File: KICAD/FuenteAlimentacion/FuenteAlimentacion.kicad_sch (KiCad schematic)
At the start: 5 parts, among them J1 USB_B_Mini, U1 LM1117DT-3.3, U2 TPS61087DSCR

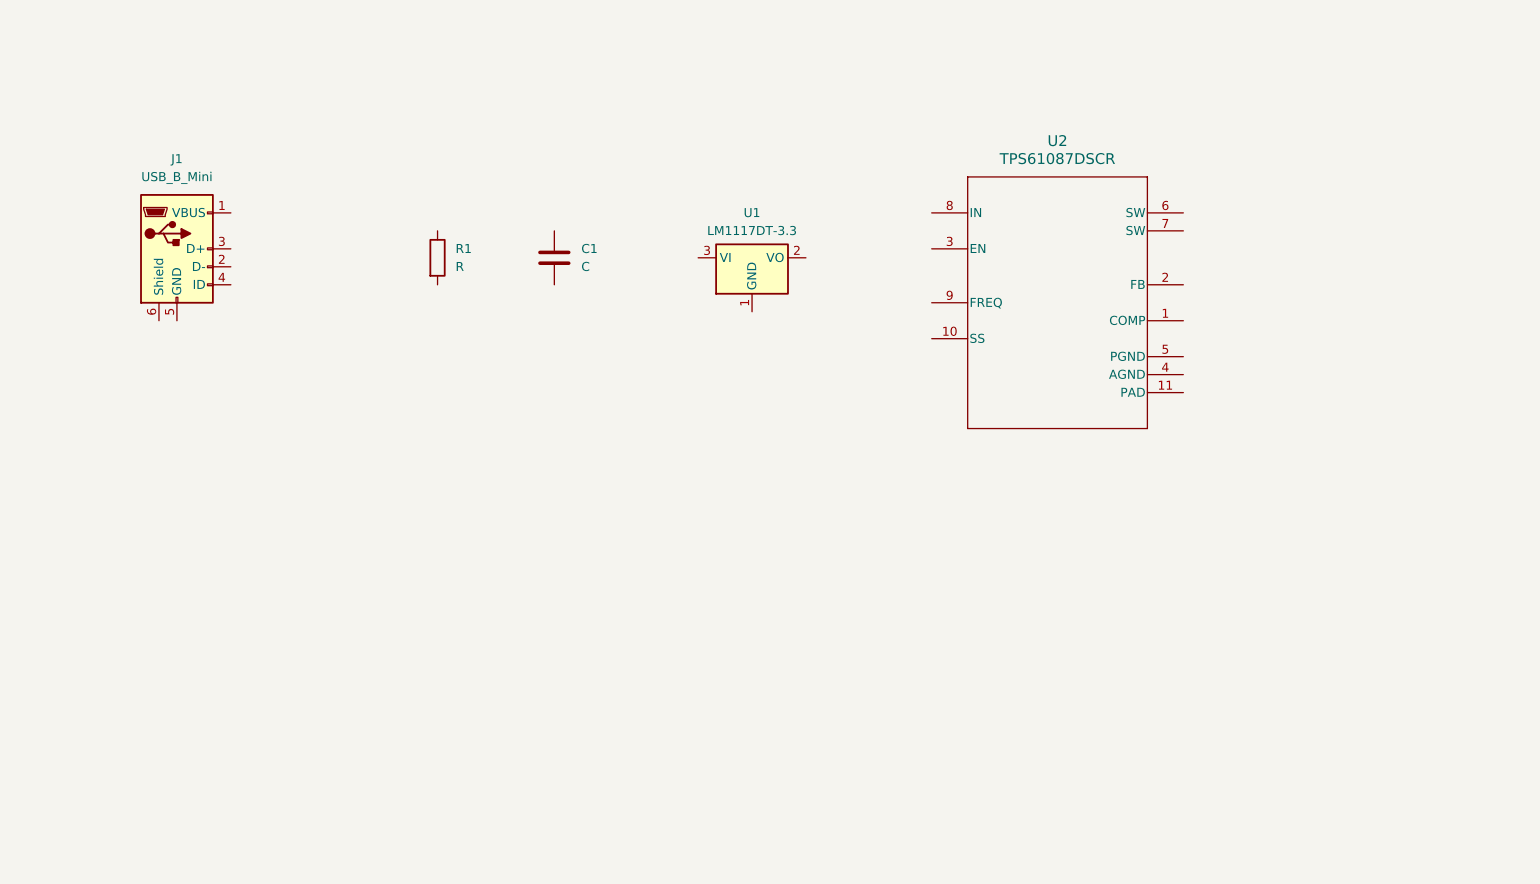
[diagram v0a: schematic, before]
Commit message: Se agrega la libreria que se proporciona para el sensor PZEM en arduino
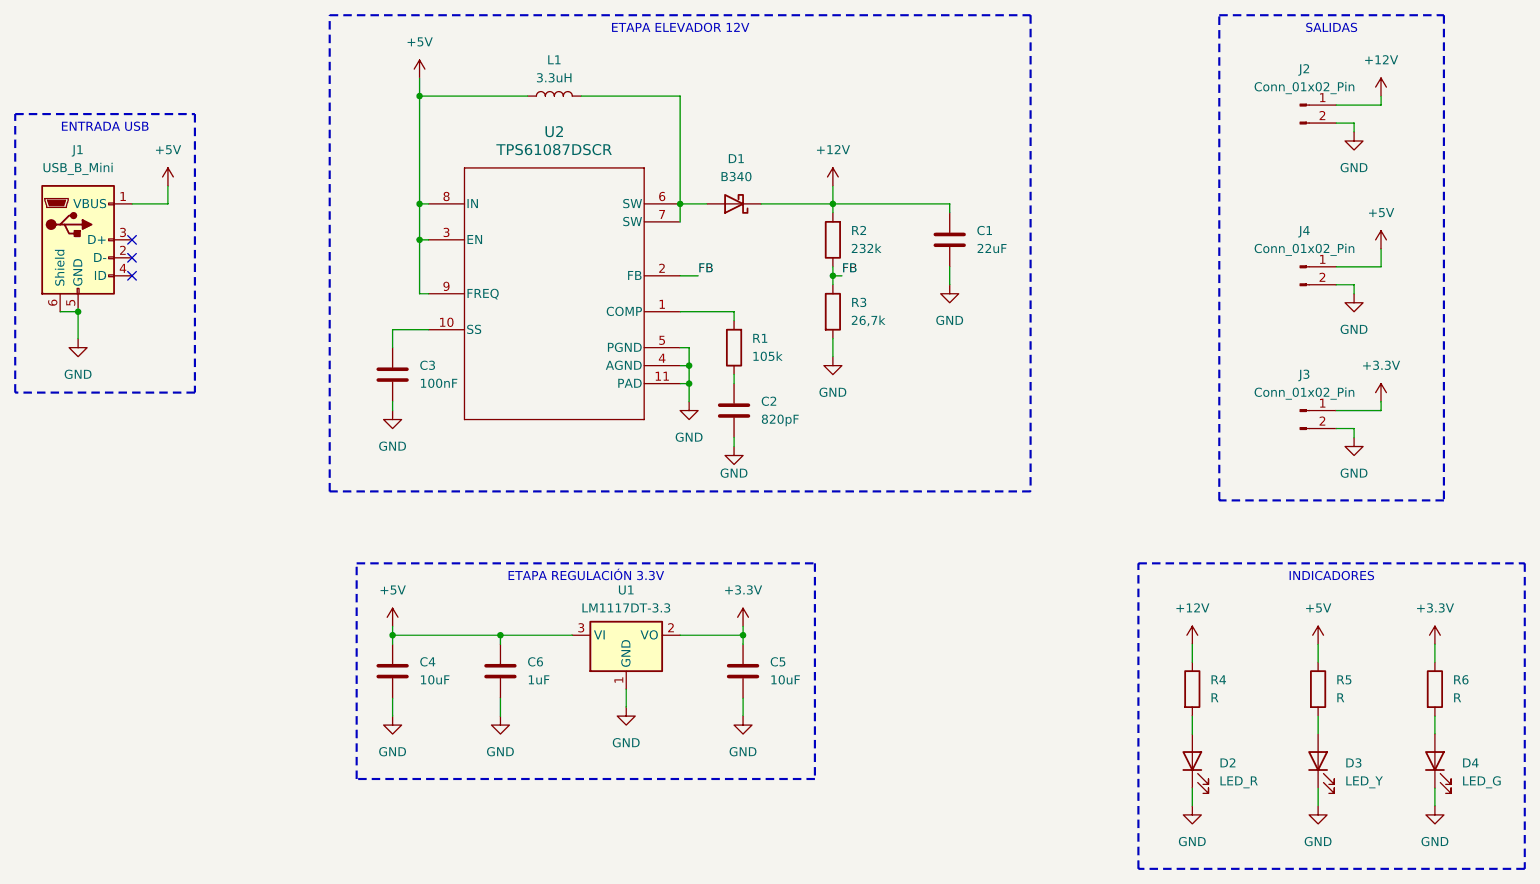
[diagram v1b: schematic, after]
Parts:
- added C2: 820pF, symbol Device:C
- added C3: 100nF, symbol Device:C
- added C4, C5: 10uF, symbol Device:C
- added C6: 1uF, symbol Device:C
- added D1: B340, Diode_SMD:D_SMC, symbol Diode:B340
- added D2: LED_R, symbol Device:LED
- added D3: LED_Y, symbol Device:LED
- added D4: LED_G, symbol Device:LED
- added J2, J3, J4: Conn_01x02_Pin, symbol Connector:Conn_01x02_Pin
- added L1: 3.3uH, symbol Device:L
- added R2: 232k, symbol Device:R
- added R3: 26,7k, symbol Device:R
- added R4, R5, R6: R, symbol Device:R
- C1: value C -> 22uF
- R1: value R -> 105k
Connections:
- net +5V: now reaches J1.1 (VBUS)
- net +5V: now also U1.3 (VI), U2.3 (EN), U2.8 (IN), U2.9 (FREQ), C4.1, C6.1, J4.1 (Pin_1), L1.1, R5.1
- net GND: now reaches J1.5 (GND)
- net GND: now also C1.1, J1.6 (Shield), U1.1 (GND), U2.11 (PAD), U2.4 (AGND), U2.5 (PGND), C2.2, C3.2, C4.2, C5.2, C6.2, D2.1 (K), D3.1 (K), D4.1 (K), J2.2 (Pin_2), J3.2 (Pin_2), J4.2 (Pin_2), R3.2
- net +3.3V: now reaches U1.2 (VO)
- net +3.3V: now also C5.1, J3.1 (Pin_1), R6.1
- net +12V: now reaches C1.2
- net +12V: now also D1.1 (K), J2.1 (Pin_1), R2.2, R4.1
- net at U2.1 (COMP): now also R1.2
- net at U2.10 (SS): now also C3.1
- net FB: now reaches U2.2 (FB)
- net FB: now also R2.1, R3.1
- net at U2.6 (SW): now also U2.7 (SW), D1.2 (A), L1.2
- net at R1.1: now also C2.1
- new net: D4.2 (A), R6.2
- new net: D3.2 (A), R5.2
- new net: D2.2 (A), R4.2
- no-connect marks 0 -> 3
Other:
- moved on the sheet: J1, U1, U2
